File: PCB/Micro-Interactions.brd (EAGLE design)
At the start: 30 x 30 mm, 6 parts

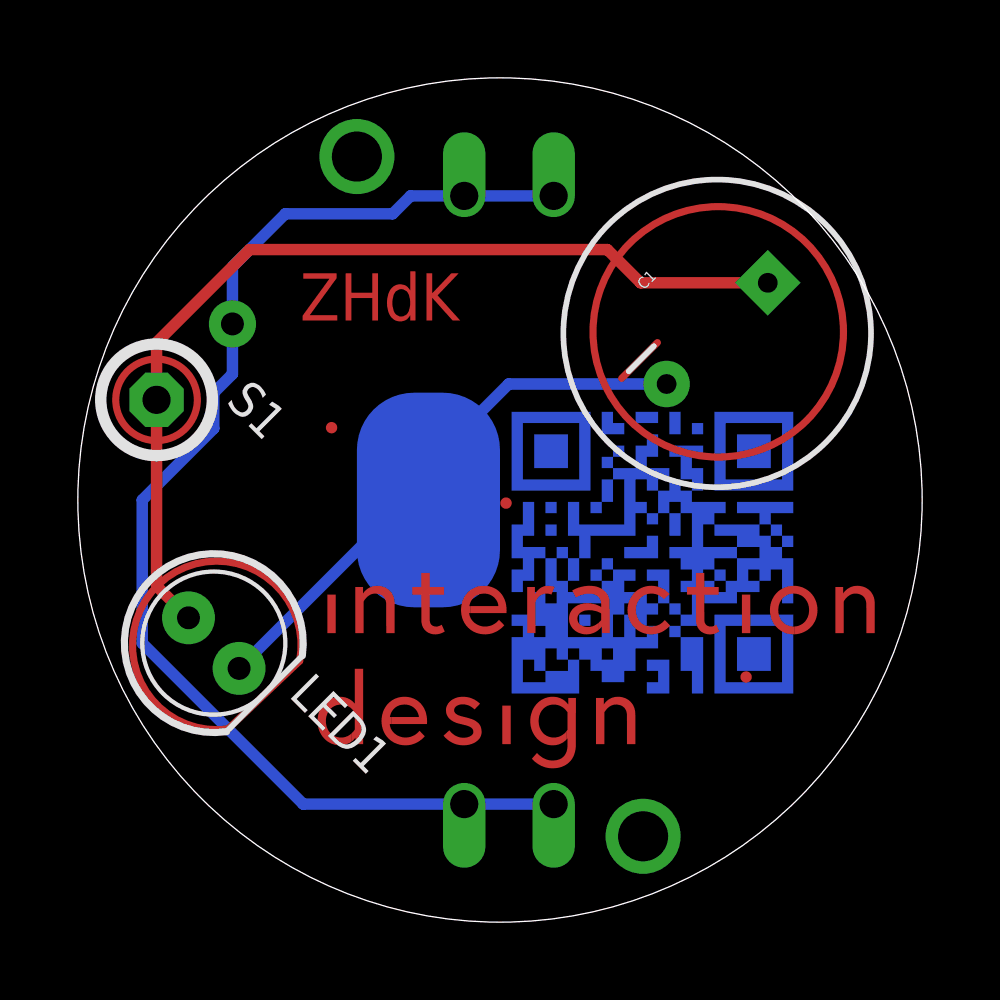
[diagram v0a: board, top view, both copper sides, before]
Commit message: Removed QR code and added web link to rear side
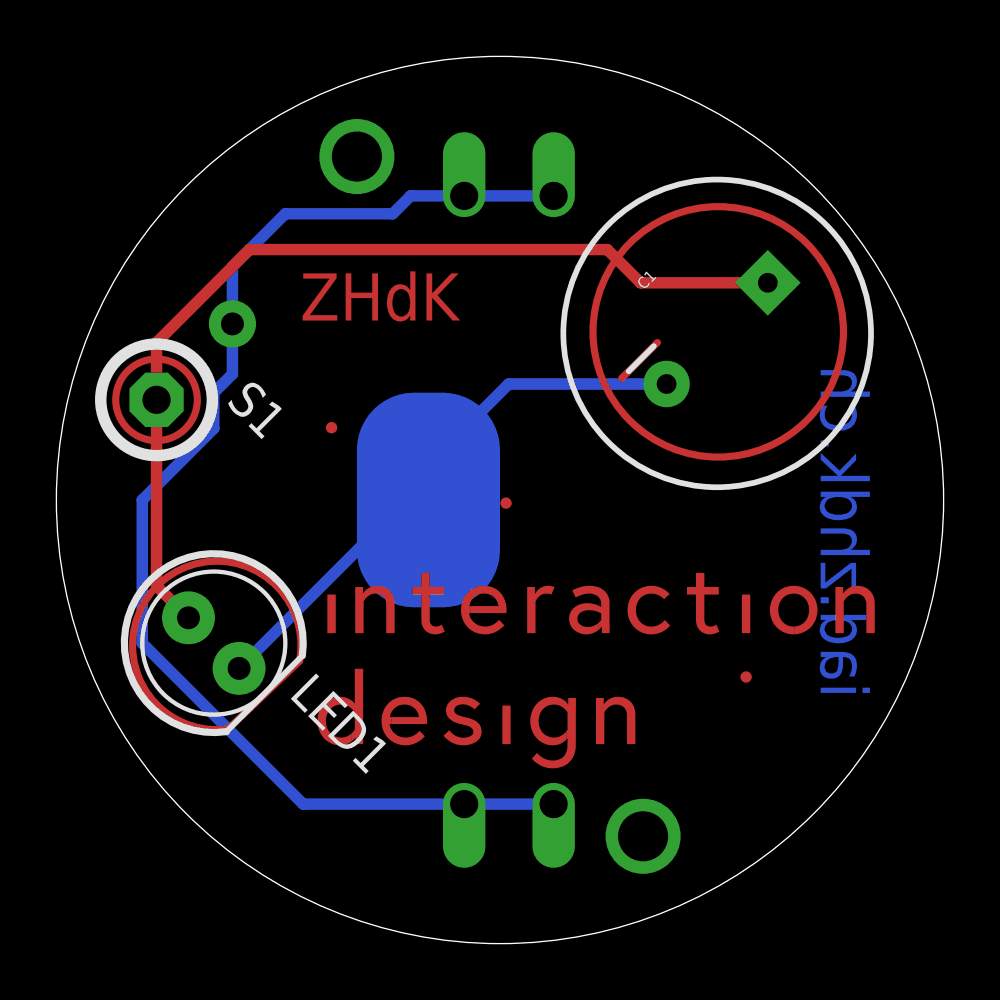
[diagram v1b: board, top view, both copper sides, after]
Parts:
- removed U$3: (no value), IAD_QRcode:IAD_QR_TDOT
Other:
- board size 30 x 30 mm -> 31.5 x 31.5 mm
- board text added: "iad.zhdk.ch"
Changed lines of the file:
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@@
 <?xml version="1.0" encoding="utf-8"?>
 <!DOCTYPE eagle SYSTEM "eagle.dtd">
-<eagle version="6.4">
+<eagle version="8.6.0">
 <drawing>
 <settings>
 <setting alwaysvectorfont="no"/>
+<setting keepoldvectorfont="yes"/>
 <setting verticaltext="up"/>
 </settings>
@@
 <layer number="19" name="Unrouted" color="6" fill="1" visible="yes" active="yes"/>
 <layer number="20" name="Dimension" color="15" fill="1" visible="yes" active="yes"/>
-<layer number="21" name="tPlace" color="16" fill="1" visible="yes" active="yes"/>
+<layer number="21" name="tPlace" color="16" fill="1" visible="no" active="yes"/>
 <layer number="22" name="bPlace" color="14" fill="1" visible="yes" active="yes"/>
 <layer number="23" name="tOrigins" color="15" fill="1" visible="yes" active="yes"/>
@@
 <board>
 <plain>
-<circle x="22.86" y="16.51" radius="14.986" width="0.002540625" layer="20"/>
+<circle x="22.86" y="16.51" radius="15.748" width="0.002540625" layer="20"/>
 <text x="21.404015625" y="24.557221875" size="1.6764" layer="1" font="vector" ratio="15" rot="R180">ZHdK</text>
 <circle x="30.607" y="22.479" radius="4.445" width="0.254" layer="1"/>
@@
 <wire x1="13.208" y1="8.382" x2="15.748" y2="10.795" width="0.254" layer="29" curve="-288.345208"/>
 <wire x1="15.748" y1="10.795" x2="13.208" y2="8.382" width="0.254" layer="29"/>
+<text x="34.243778125" y="9.466015625" size="1.6764" layer="16" font="vector" ratio="15" rot="MR90">iad.zhdk.ch</text>
 </plain>
 <attributes>
@@
 <param name="dpMaxLengthDifference" value="10mm"/>
 <param name="dpGapFactor" value="2.5"/>
-<param name="checkGrid" value="0"/>
 <param name="checkAngle" value="0"/>
 <param name="checkFont" value="1"/>
 <param name="checkRestrict" value="1"/>
+<param name="checkStop" value="0"/>
+<param name="checkValues" value="0"/>
 <param name="useDiameter" value="13"/>
 <param name="maxErrors" value="50"/>
@@
 <pass name="Default">
 <param name="RoutingGrid" value="50mil"/>
+<param name="AutoGrid" value="1"/>
+<param name="Efforts" value="0"/>
+<param name="TopRouterVariant" value="1"/>
 <param name="tpViaShape" value="round"/>
 <param name="PrefDir.1" value="|"/>
@@
 <element name="C1" library="SparkFun-Passives" package="CPOL-RADIAL-1000UF-25V" value="CAP 1000UF" x="30.5698" y="22.423753125" rot="R45"/>
 <element name="S1" library="switch-dil" package="DS-01" value="TILT_1" x="10.668" y="20.066" rot="R315">
+<attribute name="MF" value="" x="2.585771875" y="-9.56884375" size="1.778" layer="27" rot="R315" display="off"/>
+<attribute name="MPN" value="" x="2.585771875" y="-9.56884375" size="1.778" layer="27" rot="R315" display="off"/>
+<attribute name="OC_FARNELL" value="unknown" x="2.585771875" y="-9.56884375" size="1.778" layer="27" rot="R315" display="off"/>
 <attribute name="OC_NEWARK" value="unknown" x="2.585771875" y="-9.56884375" size="1.778" layer="27" rot="R315" display="off"/>
-<attribute name="MPN" value="" x="2.585771875" y="-9.56884375" size="1.778" layer="27" rot="R315" display="off"/>
-<attribute name="MF" value="" x="2.585771875" y="-9.56884375" size="1.778" layer="27" rot="R315" display="off"/>
-<attribute name="OC_FARNELL" value="unknown" x="2.585771875" y="-9.56884375" size="1.778" layer="27" rot="R315" display="off"/>
 </element>
 <element name="U$1" library="20mm_cell_throughholl" package="BATTCON_20MM_4LEGS" value="BATTCELL_20MM_THROUGHHOLE" x="22.86" y="16.51" rot="MR270"/>
 <element name="U$2" library="IADLOGO_20MM" package="IADLOGO_20MM" value="" x="14.478" y="6.223"/>
-<element name="U$3" library="IAD_QRcode" package="IAD_QR_TDOT" value="" x="33.782" y="19.812" rot="MR0"/>
 </elements>
 <signals>
@@
 <via x="17.78" y="28.702" extent="1-16" drill="1.778" diameter="0.0254"/>
 <via x="27.94" y="4.572" extent="1-16" drill="1.778" diameter="0.0254"/>
+<wire x1="27.94" y1="4.572" x2="17.78" y2="28.702" width="0" layer="19" extent="1-1"/>
 </signal>
 </signals>
